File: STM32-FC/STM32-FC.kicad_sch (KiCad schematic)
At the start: 13 parts, among them IC1 STM32F746NGH6, J1 SM06B-GHS-TBT, Y1 16MHz

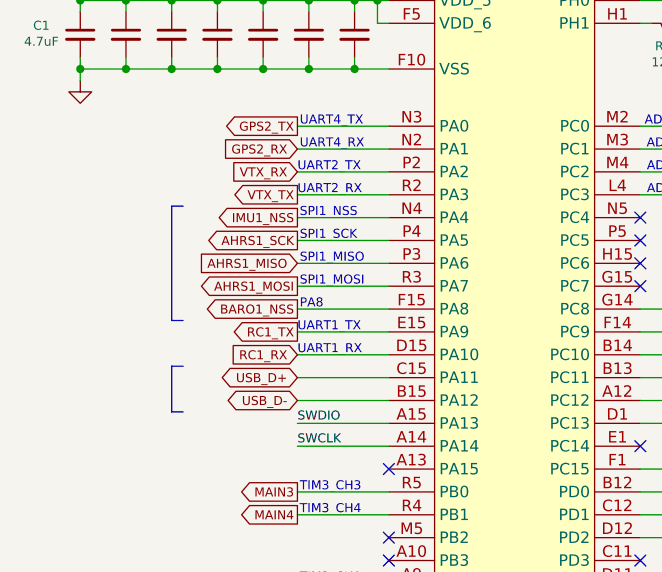
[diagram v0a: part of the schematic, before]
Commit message: fix : STM32 USB & VTX
- USB DM/DP 결선 수정
- VTX RX/TX 수정
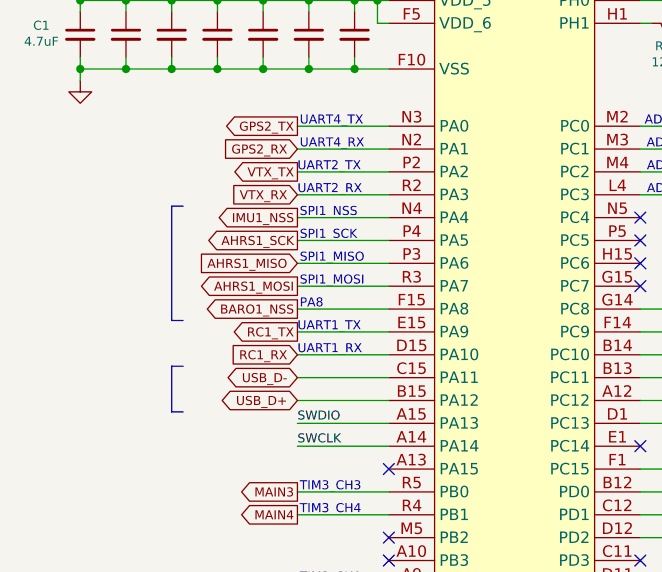
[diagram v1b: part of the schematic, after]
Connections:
- net USB_D+: now also IC1.B15 (PA12); no longer IC1.C15 (PA11)
- net USB_D-: now also IC1.C15 (PA11); no longer IC1.B15 (PA12)
- net VTX_RX: now also IC1.R2 (PA3); no longer IC1.P2 (PA2)
- net VTX_TX: now also IC1.P2 (PA2); no longer IC1.R2 (PA3)
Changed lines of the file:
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@@
 	(global_label "USB_D+"
 		(shape bidirectional)
-		(at 64.77 80.01 180)
-		(fields_autoplaced yes)
-		(effects
-			(font
-				(size 1 1)
-			)
-			(justify right)
-		)
-		(property "Intersheetrefs" "${INTERSHEET_REFS}"
-			(at 55.5447 80.01 0)
+		(at 64.77 82.55 180)
+		(fields_autoplaced yes)
+		(effects
+			(font
+				(size 1 1)
+			)
+			(justify right)
+		)
+		(property "Intersheetrefs" "${INTERSHEET_REFS}"
+			(at 55.5447 82.55 0)
 			(effects
 				(font
@@
 	(global_label "USB_D-"
 		(shape bidirectional)
-		(at 64.77 82.55 180)
-		(fields_autoplaced yes)
-		(effects
-			(font
-				(size 1 1)
-			)
-			(justify right)
-		)
-		(property "Intersheetrefs" "${INTERSHEET_REFS}"
-			(at 55.5447 82.55 0)
+		(at 64.77 80.01 180)
+		(fields_autoplaced yes)
+		(effects
+			(font
+				(size 1 1)
+			)
+			(justify right)
+		)
+		(property "Intersheetrefs" "${INTERSHEET_REFS}"
+			(at 55.5447 80.01 0)
 			(effects
 				(font
@@
 	(global_label "VTX_RX"
 		(shape input)
+		(at 64.77 59.69 180)
+		(fields_autoplaced yes)
+		(effects
+			(font
+				(size 1 1)
+			)
+			(justify right)
+		)
+		(property "Intersheetrefs" "${INTERSHEET_REFS}"
+			(at 57.134 59.69 0)
+			(effects
+				(font
+					(size 1.27 1.27)
+				)
+				(justify right)
+				(hide yes)
+			)
+		)
+	)
+	(global_label "VTX_TX"
+		(shape output)
 		(at 64.77 57.15 180)
 		(fields_autoplaced yes)
@@
 		)
 		(property "Intersheetrefs" "${INTERSHEET_REFS}"
-			(at 57.134 57.15 0)
-			(effects
-				(font
-					(size 1.27 1.27)
-				)
-				(justify right)
-				(hide yes)
-			)
-		)
-	)
-	(global_label "VTX_TX"
-		(shape output)
-		(at 64.77 59.69 180)
-		(fields_autoplaced yes)
-		(effects
-			(font
-				(size 1 1)
-			)
-			(justify right)
-		)
-		(property "Intersheetrefs" "${INTERSHEET_REFS}"
-			(at 57.3721 59.69 0)
-			(effects
-				(font
+			(at 57.3721 57.15 0)
+			(effects
+				(font

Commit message: init:footprint
footprint 작업 시작
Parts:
- IC1: footprint BGA216C80P15X15_1300X1300X110 -> STM32F746NGH6:STM32F746NGH6
- J1: footprint JST_GH:JST_GH_SM06B-GHS-TB_06x1.25mm_Angled -> Connector_JST:JST_GH_SM06B-GHS-TB_1x06-1MP_P1.25mm_Horizontal
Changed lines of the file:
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@@
 			)
 		)
-		(property "Footprint" "BGA216C80P15X15_1300X1300X110"
+		(property "Footprint" "STM32F746NGH6:STM32F746NGH6"
 			(at 88.9 78.74 0)
 			(effects
@@
 			)
 		)
-		(property "Footprint" "JST_GH:JST_GH_SM06B-GHS-TB_06x1.25mm_Angled"
+		(property "Footprint" "Connector_JST:JST_GH_SM06B-GHS-TB_1x06-1MP_P1.25mm_Horizontal"
 			(at 252.73 33.02 0)
 			(effects

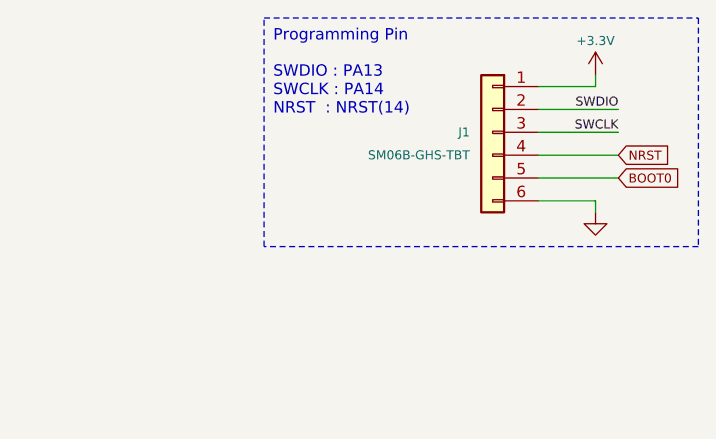
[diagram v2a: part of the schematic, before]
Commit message: update : BOM and minor fix
- remove : DC2DC for analog
- change : JST SM conn. to BM
- change : ELRS conn. to JST XH (instead of JST SM)
- update : BOM List
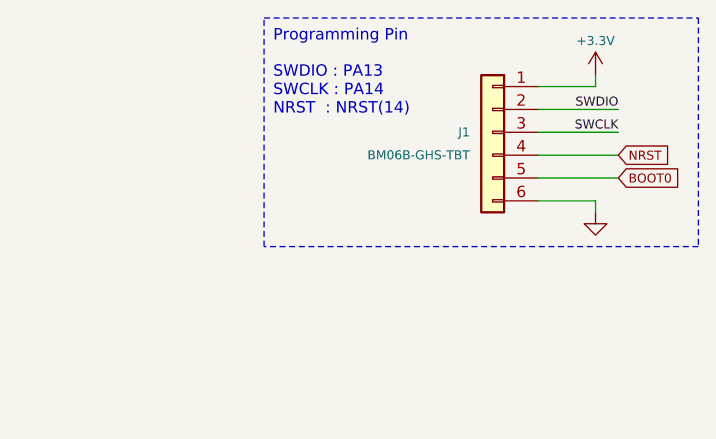
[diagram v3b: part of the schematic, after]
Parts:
- C1: LCSC C307415 -> C307423
- IC1: LCSC (none) -> C503080
- J1: value SM06B-GHS-TBT -> BM06B-GHS-TBT; footprint Connector_JST:JST_GH_SM06B-GHS-TB_1x06-1MP_P1.25mm_Horizontal -> Connector_JST:JST_GH_BM06B-GHS-TBT_1x06-1MP_P1.25mm_Vertical; LCSC C133065 -> C189892
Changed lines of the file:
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@@
 			)
 		)
-		(property "LCSC" "C307415"
+		(property "LCSC" "C307423"
 			(at 43.18 40.6462 0)
 			(effects
@@
 			)
 		)
+		(property "LCSC" "C503080"
+			(at 88.9 78.74 0)
+			(effects
+				(font
+					(size 1.27 1.27)
+				)
+				(hide yes)
+			)
+		)
 		(pin "E9"
 		)
@@
 			)
 		)
-		(property "Value" "SM06B-GHS-TBT"
+		(property "Value" "BM06B-GHS-TBT"
 			(at 250.19 35.56 0)
 			(effects
@@
 			)
 		)
-		(property "Footprint" "Connector_JST:JST_GH_SM06B-GHS-TB_1x06-1MP_P1.25mm_Horizontal"
+		(property "Footprint" "Connector_JST:JST_GH_BM06B-GHS-TBT_1x06-1MP_P1.25mm_Vertical"
 			(at 252.73 33.02 0)
 			(effects
@@
 			)
 		)
-		(property "LCSC" "C133065"
+		(property "LCSC" "C189892"
 			(at 252.73 33.02 0)
 			(effects

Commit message: change : RC size 0402 to 0201
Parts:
- C2, C3, C4, C5, C6, C7: footprint Capacitor_SMD:C_0402_1005Metric -> Capacitor_SMD:C_0201_0603Metric; LCSC C1525 -> C49062
- C8, C9: footprint Capacitor_SMD:C_0402_1005Metric -> Capacitor_SMD:C_0201_0603Metric; LCSC C1545 -> C384956
- R1: footprint Resistor_SMD:R_0402_1005Metric -> Resistor_SMD:R_0201_0603Metric; LCSC C25079 -> C295718
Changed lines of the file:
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@@
 			)
 		)
-		(property "Footprint" "Resistor_SMD:R_0402_1005Metric"
+		(property "Footprint" "Resistor_SMD:R_0201_0603Metric"
 			(at 106.68 40.64 0)
 			(effects
@@
 			)
 		)
-		(property "Description" "Resistor, small US symbol"
+		(property "Description" "-55℃~+125℃ 120Ω 25V 50mW Thick Film Resistor ±1% ±200ppm/℃ 0201 Chip Resistor - Surface Mount ROHS"
 			(at 106.68 40.64 0)
 			(effects
@@
 			)
 		)
-		(property "LCSC" " C25079"
+		(property "LCSC" "C295718"
 			(at 106.68 40.64 0)
 			(effects
@@
 			)
 		)
-		(property "Footprint" "Capacitor_SMD:C_0402_1005Metric"
+		(property "Footprint" "Capacitor_SMD:C_0201_0603Metric"
 			(at 55.88 41.91 0)
 			(effects
@@
 			)
 		)
-		(property "Description" "Unpolarized capacitor, small symbol"
+		(property "Description" "100nF 10V X5R ±10% 0201 Multilayer Ceramic Capacitors MLCC - SMD/SMT ROHS"
 			(at 55.88 41.91 0)
 			(effects
@@
 			)
 		)
-		(property "LCSC" "C1525"
+		(property "LCSC" "C49062"
 			(at 53.34 40.6462 0)
 			(effects
@@
 			)
 		)
-		(property "Footprint" "Capacitor_SMD:C_0402_1005Metric"
+		(property "Footprint" "Capacitor_SMD:C_0201_0603Metric"
 			(at 71.12 41.91 0)
 			(effects
@@
 			)
 		)
-		(property "Description" "Unpolarized capacitor, small symbol"
+		(property "Description" "100nF 10V X5R ±10% 0201 Multilayer Ceramic Capacitors MLCC - SMD/SMT ROHS"
 			(at 71.12 41.91 0)
 			(effects
@@
 			)
 		)
-		(property "LCSC" "C1525"
+		(property "LCSC" "C49062"
 			(at 68.58 40.6462 0)
 			(effects
@@
 			)
 		)
-		(property "Footprint" "Capacitor_SMD:C_0402_1005Metric"
+		(property "Footprint" "Capacitor_SMD:C_0201_0603Metric"
 			(at 66.04 41.91 0)
 			(effects
@@
 			)
 		)
-		(property "Description" "Unpolarized capacitor, small symbol"
+		(property "Description" "100nF 10V X5R ±10% 0201 Multilayer Ceramic Capacitors MLCC - SMD/SMT ROHS"
 			(at 66.04 41.91 0)
 			(effects
@@
 			)
 		)
-		(property "LCSC" "C1525"
+		(property "LCSC" "C49062"
 			(at 63.5 40.6462 0)
 			(effects
@@
 			)
 		)
-		(property "Footprint" "Capacitor_SMD:C_0402_1005Metric"
+		(property "Footprint" "Capacitor_SMD:C_0201_0603Metric"
 			(at 50.8 41.91 0)
 			(effects
@@
 			)
 		)
-		(property "Description" "Unpolarized capacitor, small symbol"
+		(property "Description" "100nF 10V X5R ±10% 0201 Multilayer Ceramic Capacitors MLCC - SMD/SMT ROHS"
 			(at 50.8 41.91 0)
 			(effects
@@
 			)
 		)
-		(property "LCSC" "C1525"
+		(property "LCSC" "C49062"
 			(at 48.26 40.6462 0)
 			(effects
@@
 			)
 		)
-		(property "Footprint" "Capacitor_SMD:C_0402_1005Metric"
+		(property "Footprint" "Capacitor_SMD:C_0201_0603Metric"
 			(at 45.72 41.91 0)
 			(effects
@@
 			)
 		)
-		(property "Description" "Unpolarized capacitor, small symbol"
+		(property "Description" "100nF 10V X5R ±10% 0201 Multilayer Ceramic Capacitors MLCC - SMD/SMT ROHS"
 			(at 45.72 41.91 0)
 			(effects
@@
 			)
 		)
-		(property "LCSC" "C1525"
+		(property "LCSC" "C49062"
 			(at 43.18 40.6462 0)
 			(effects
@@
 			)
 		)
-		(property "Footprint" "Capacitor_SMD:C_0402_1005Metric"
+		(property "Footprint" "Capacitor_SMD:C_0201_0603Metric"
 			(at 60.96 41.91 0)
 			(effects
@@
 			)
 		)
-		(property "Description" "Unpolarized capacitor, small symbol"
+		(property "Description" "100nF 10V X5R ±10% 0201 Multilayer Ceramic Capacitors MLCC - SMD/SMT ROHS"
 			(at 60.96 41.91 0)
 			(effects
@@
 			)
 		)
-		(property "LCSC" "C1525"
+		(property "LCSC" "C49062"
 			(at 58.42 40.6462 0)
 			(effects
@@
 			)
 		)
-		(property "Footprint" "Capacitor_SMD:C_0402_1005Metric"
+		(property "Footprint" "Capacitor_SMD:C_0201_0603Metric"
 			(at 125.73 44.45 0)
 			(effects
@@
 			)
 		)
-		(property "Description" "Unpolarized capacitor, small symbol"
+		(property "Description" "10pF 50V C0G ±1% 0201 Multilayer Ceramic Capacitors MLCC - SMD/SMT ROHS"
 			(at 125.73 44.45 0)
 			(effects
@@
 			)
 		)
-		(property "LCSC" "C1545"
+		(property "LCSC" "C384956"
 			(at 125.73 44.45 0)
 			(effects
@@
 			)
 		)
-		(property "Footprint" "Capacitor_SMD:C_0402_1005Metric"
+		(property "Footprint" "Capacitor_SMD:C_0201_0603Metric"
 			(at 113.03 44.45 0)
 			(effects
@@
 			)
 		)
-		(property "Description" "Unpolarized capacitor, small symbol"
+		(property "Description" "10pF 50V C0G ±1% 0201 Multilayer Ceramic Capacitors MLCC - SMD/SMT ROHS"
 			(at 113.03 44.45 0)
 			(effects
@@
 			)
 		)
-		(property "LCSC" "C1545"
+		(property "LCSC" "C384956"
 			(at 113.03 44.45 0)
 			(effects
